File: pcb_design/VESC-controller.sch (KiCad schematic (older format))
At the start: 33 parts, among them J1 GATE_DRIVER_CONN_U, J2 GATE_DRIVER_CONN_V, J3 GATE_DRIVER_CONN_W, J4 micro USB, J5 ACCEL, J6 REGEN, J7 12V, J8 V_BUS, P1 HALL/Encoder, P101 CANBUS, P2 Resolver, P3 PWR_COMM

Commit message: Completed some part numbers
Signed-off-by: Marcos Chaparro <mchaparro@paltatech.com>
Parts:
- C66, C67, C68: MFR (none) -> Murata Electronics North America; MPN (none) -> GRM21BR71A475KA73K; SPN (none) -> 490-6479-1-ND; SPR (none) -> Digikey
- C69, C70, C71: MFR (none) -> Murata Electronics North America; MPN (none) -> GRM31CR71H475KA12L; SPN (none) -> 490-6521-1-ND; SPR (none) -> Digikey

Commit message: Completed part number, manufacturer, etc fields. Simulated analog conditioning
Signed-off-by: Marcos Chaparro <mchaparro@paltatech.com>
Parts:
- D21, D22: MFR (none) -> Toshiba Semiconductor and Storage; MPN (none) -> TBAT54S,LM; SPN (none) -> TBAT54SLMCT-ND; SPR (none) -> Digikey
- DS1, DS5: MFR (none) -> Lite-On Inc.; MPN (none) -> LTST-C191KRKT; SPN (none) -> 160-1447-1-ND; SPR (none) -> Digikey
- DS2, DS4: MFR (none) -> Lite-On Inc.; MPN (none) -> LTST-C191KGKT; SPN (none) -> 160-1446-1-ND; SPR (none) -> Digikey
- J1, J2, J3: MFR (none) -> Amphenol FCI; MPN (none) -> 67997-216HLF; SPN (none) -> 609-3238-ND; SPR (none) -> Digikey
- J4: MFR (none) -> Amphenol FCI; MPN (none) -> 10118194-0001LF; SPN (none) -> 609-4618-1-ND; SPR (none) -> Digikey
- J5, J6: MFR (none) -> Phoenix Contact; MPN (none) -> 1803439; SPN (none) -> 277-1222-ND; SPR (none) -> Digikey
- J7: MFR (none) -> Phoenix Contact; MPN (none) -> 1803426; SPN (none) -> 277-1221-ND; SPR (none) -> Digikey
- J8: MFR (none) -> Phoenix Contact; MPN (none) -> 1803442; SPN (none) -> 277-1223-ND; SPR (none) -> Digikey
- P1, P2: MFR (none) -> Phoenix Contact; MPN (none) -> 1803468; SPN (none) -> 277-1225-ND; SPR (none) -> Digikey
- P101: MFR (none) -> JST Sales America Inc.; MPN (none) -> B4B-PH-K-S(LF)(SN); SPN (none) -> 455-1706-ND; SPR (none) -> Digikey
- P3: MFR (none) -> Phoenix Contact; MPN (none) -> 1803471; SPN (none) -> 277-1226-ND; SPR (none) -> Digikey
- R103, R104: MFR (none) -> Yageo; MPN (none) -> RC0603FR-0722RL; SPN (none) -> 311-22.0HRCT-ND; SPR (none) -> Digikey
- R11, R134, R135, R38: MFR (none) -> Yageo; MPN (none) -> RC0603FR-07100RL; SPN (none) -> 311-100HRCT-ND; SPR (none) -> Digikey
- R139: MFR (none) -> Yageo; MPN (none) -> RC0603FR-071KL; SPN (none) -> 311-1.00KHRCT-ND; SPR (none) -> Digikey
- R140: MFR (none) -> Yageo; MPN (none) -> RC0603FR-0710KL; SPN (none) -> 311-10.0KHRCT-ND; SPR (none) -> Digikey
- R6: MFR (none) -> Yageo; MPN (none) -> RC0603JR-070RL; SPN (none) -> 311-0.0GRCT-ND; SPR (none) -> Digikey

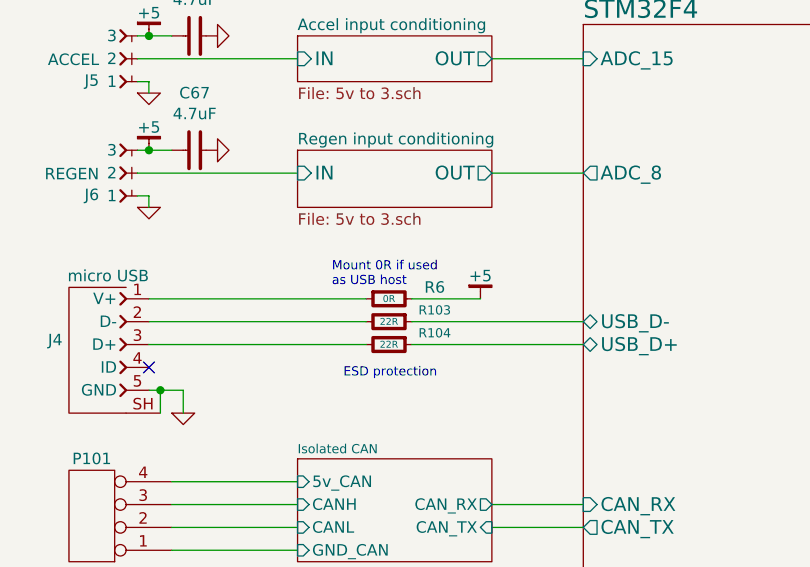
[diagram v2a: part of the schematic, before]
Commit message: Corrected phase current gain. More 3d models
Signed-off-by: Marcos Chaparro <mchaparro@paltatech.com>
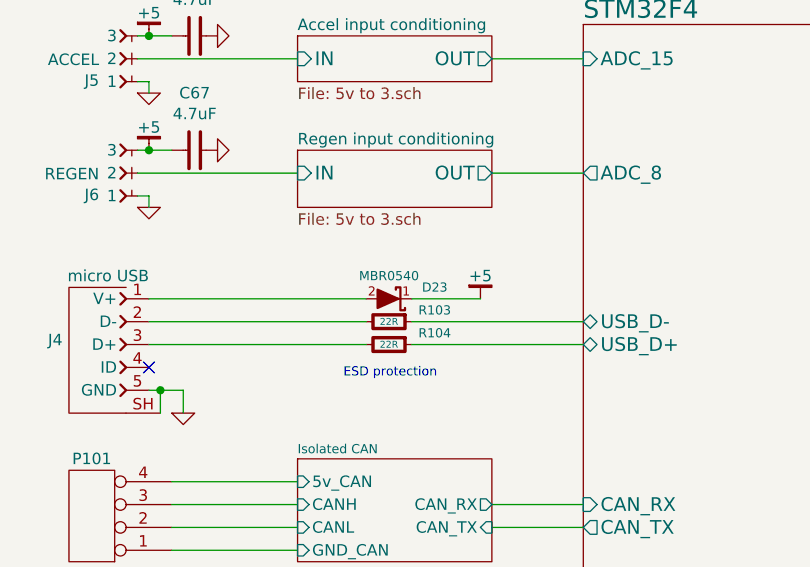
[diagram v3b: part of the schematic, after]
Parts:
- removed R6: 0R, IPC7351-Nominal:RESC1608X50, symbol R-0603
- added D23: MBR0540, smd-semi:SOD-123, symbol MBR0540
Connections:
- net +5: now also D23.1 (K)
- net at J4.1 (V+): now also D23.2 (A)
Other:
- note removed: "Mount 0R if used\nas USB host"

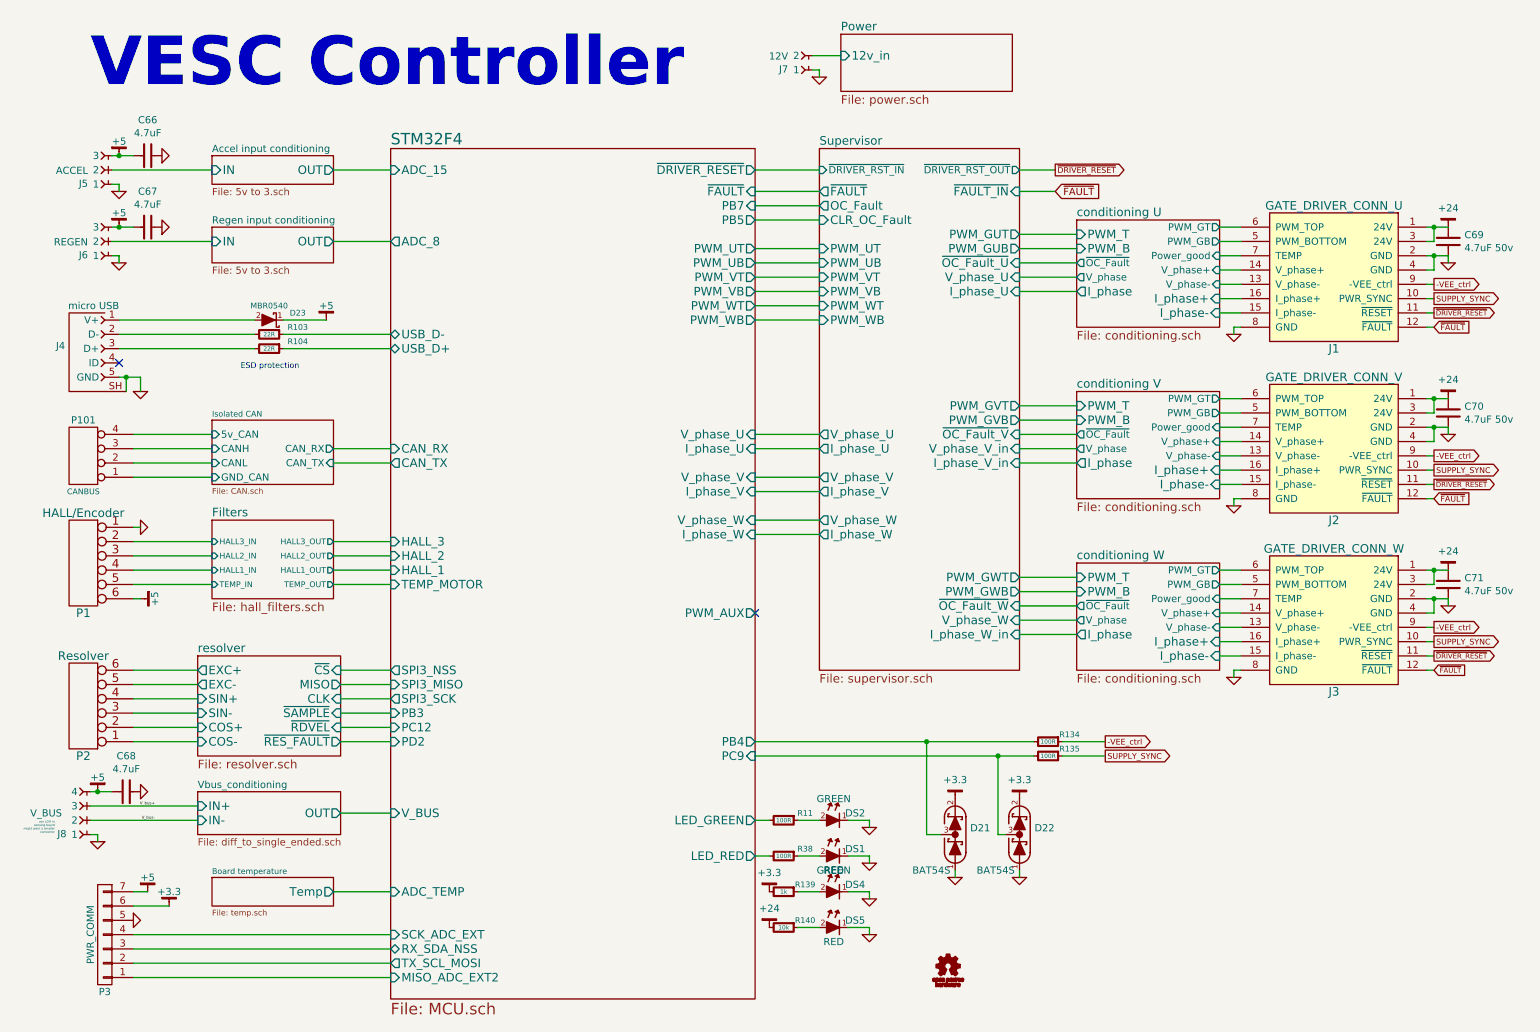
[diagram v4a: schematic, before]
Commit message: Added individual temperature sensing for each half bridge and 2 pwm gpio with low side driver
Signed-off-by: Marcos Chaparro <mchaparro@paltatech.com>
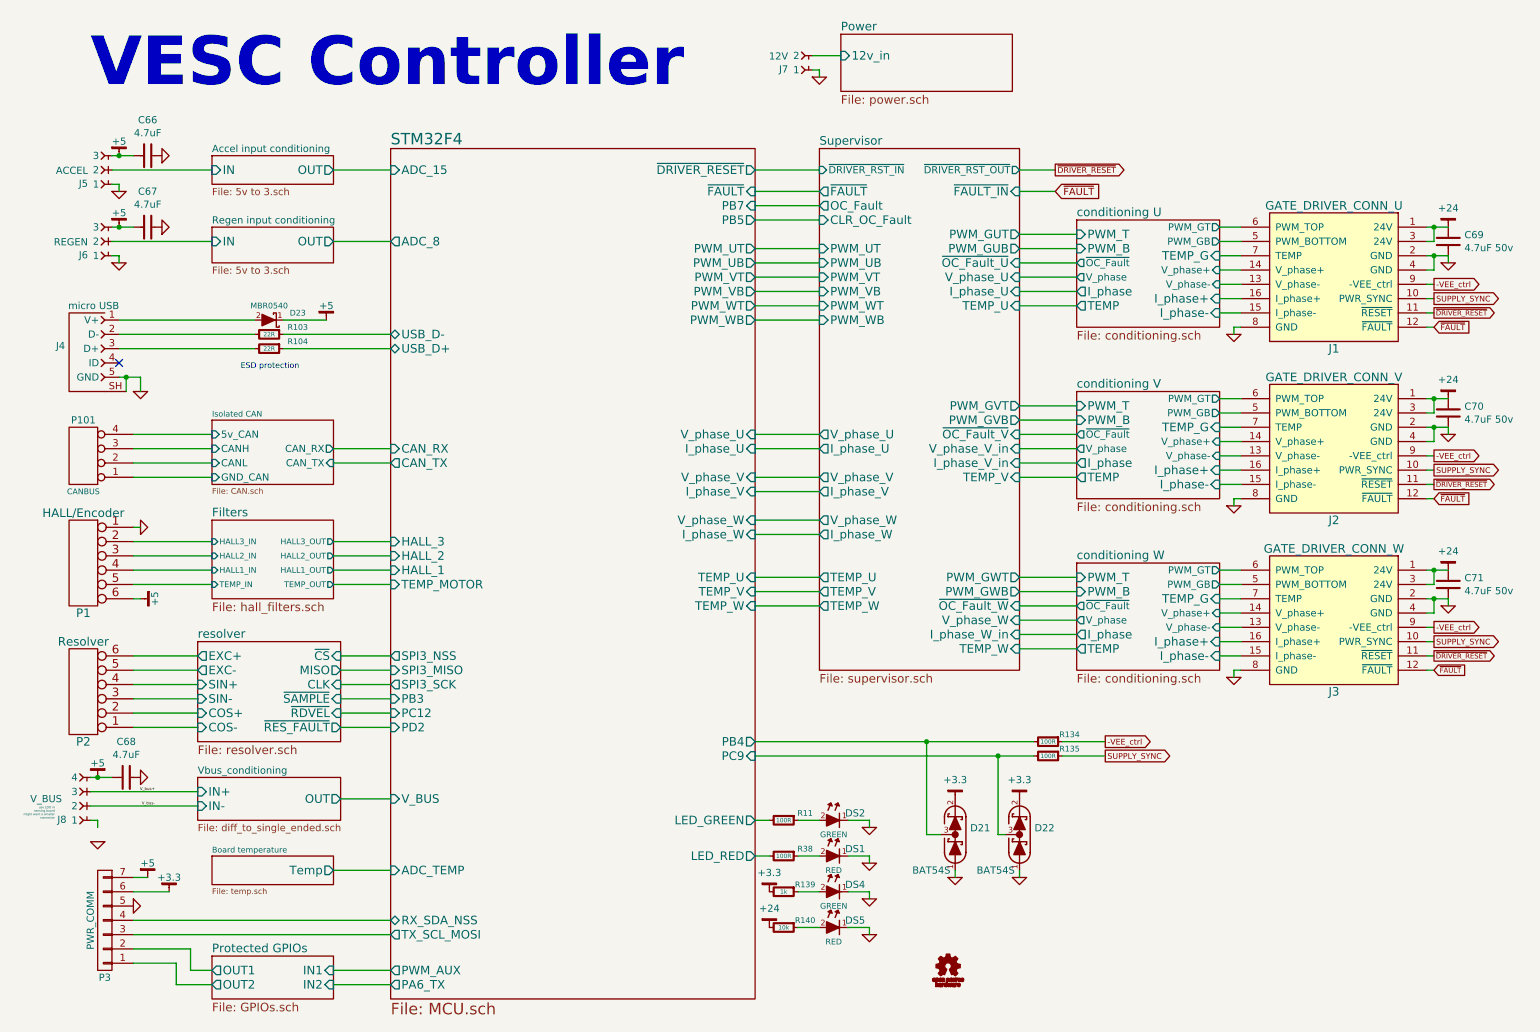
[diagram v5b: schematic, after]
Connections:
- net STM32F4/SCK_ADC_EXT is gone; now on net STM32F4/RX_SDA_NSS: P3.4 (P4)
- net GND: no longer J8.1
- net STM32F4/RX_SDA_NSS: no longer P3.3 (P3)
- net STM32F4/TX_SCL_MOSI: now also P3.3 (P3); no longer P3.2 (P2)
- net STM32F4/MISO_ADC_EXT2 renamed Protected GPIOs/OUT2
- net conditioning U/Power_good renamed conditioning U/TEMP_G
- net conditioning V/Power_good renamed conditioning V/TEMP_G
- net conditioning W/Power_good renamed conditioning W/TEMP_G
- new net Protected GPIOs/OUT1: P3.2 (P2)
- no-connect marks 2 -> 1
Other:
- moved on the sheet: C68, J8, P2, P3

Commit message: Fixed power supply inductor footprints in the layout
Signed-off-by: Marcos Chaparro <mchaparro@paltatech.com>
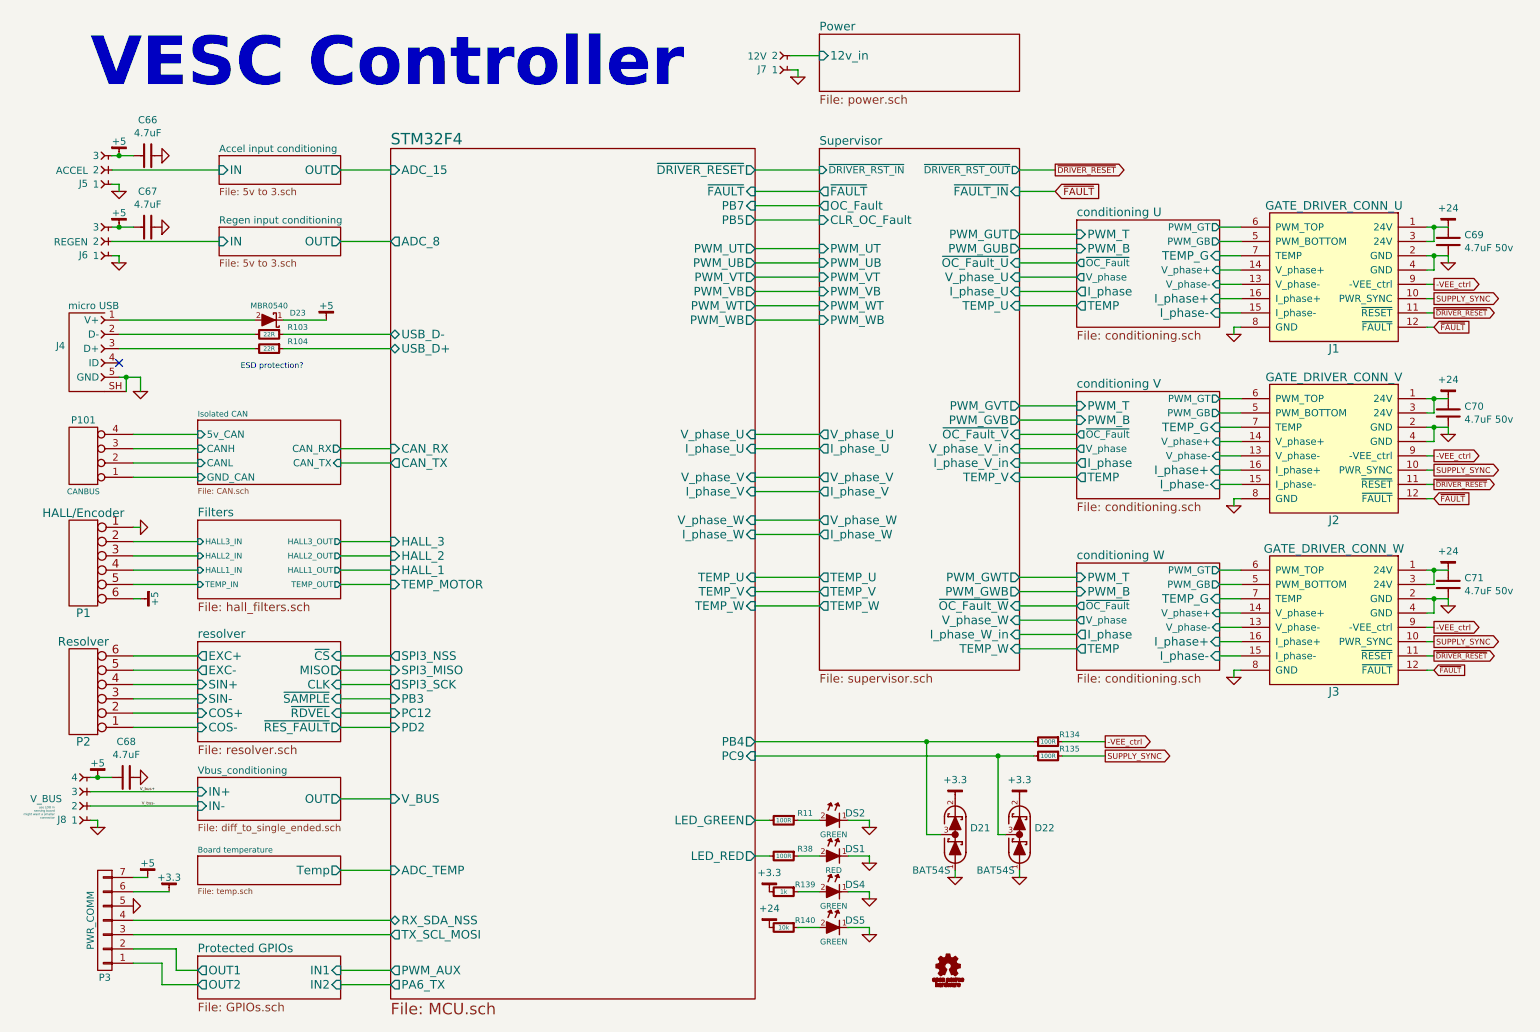
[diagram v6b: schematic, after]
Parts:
- DS5: value RED -> GREEN; MPN LTST-C191KRKT -> LTST-C191KGKT; SPN 160-1447-1-ND -> 160-1446-1-ND
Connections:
- net GND: now also J8.1
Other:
- note added: "ESD protection?"
- note removed: "ESD protection\n"
- moved on the sheet: J7

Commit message: Added RC filter to FAULT line to prevent noise triggering it
Signed-off-by: Marcos Chaparro <mchaparro@paltatech.com>
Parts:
- R103, R104: BOM (none) -> RES SMD 22 1% [0603]; mfg# RC0603FR-0722RL -> (none)
- R11, R134, R135, R38: BOM (none) -> RES SMD 1k 5% [0603]; mfg# RC0603FR-07100RL -> (none)
- R139, R140: BOM (none) -> RES SMD 1k 5% [0603]
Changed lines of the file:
@@
 F 2 "IPC7351-Nominal:RESC1608X50" V 2330 2750 30  0001 C CNN
 F 3 "" H 2400 2750 30  0001 C CNN
-F 4 "RC0603FR-0722RL" H 2400 2750 60  0001 C CNN "mfg#"
+F 4 "" H 2400 2750 60  0001 C CNN "mfg#"
 F 5 "Yageo" H 0   0   50  0001 C CNN "MFR"
 F 6 "RC0603FR-0722RL" H 0   0   50  0001 C CNN "MPN"
@@
 F 8 "311-22.0HRCT-ND" H 0   0   50  0001 C CNN "SPN"
 F 9 "" H 0   0   50  0001 C CNN "SPURL"
+F 10 "RES SMD 22 1% [0603]" H 0   0   60  0001 C CNN "BOM"
 	1    2400 2750
 	0    1    1    0
@@
 F 2 "IPC7351-Nominal:RESC1608X50" V 2330 2850 30  0001 C CNN
 F 3 "" H 2400 2850 30  0001 C CNN
-F 4 "RC0603FR-0722RL" H 2400 2850 60  0001 C CNN "mfg#"
+F 4 "" H 2400 2850 60  0001 C CNN "mfg#"
 F 5 "Yageo" H 0   0   50  0001 C CNN "MFR"
 F 6 "RC0603FR-0722RL" H 0   0   50  0001 C CNN "MPN"
@@
 F 8 "311-22.0HRCT-ND" H 0   0   50  0001 C CNN "SPN"
 F 9 "" H 0   0   50  0001 C CNN "SPURL"
+F 10 "RES SMD 22 1% [0603]" H 0   0   60  0001 C CNN "BOM"
 	1    2400 2850
 	0    1    1    0
@@
 F 2 "IPC7351-Nominal:RESC1608X50" V 5930 6400 30  0001 C CNN
 F 3 "http://www.yageo.com/NewPortal/yageodocoutput?fileName=/pdf/R-Chip/PYu-RC_Group_51_RoHS_L_4.pdf" H 6000 6400 30  0001 C CNN
-F 4 "RC0603FR-07100RL" H 6000 6400 60  0001 C CNN "mfg#"
+F 4 "" H 6000 6400 60  0001 C CNN "mfg#"
 F 5 "Yageo" H 0   0   50  0001 C CNN "MFR"
 F 6 "RC0603FR-07100RL" H 0   0   50  0001 C CNN "MPN"
@@
 F 8 "311-100HRCT-ND" H 0   0   50  0001 C CNN "SPN"
 F 9 "" H 0   0   50  0001 C CNN "SPURL"
+F 10 "RES SMD 1k 5% [0603]" H 0   0   60  0001 C CNN "BOM"
 	1    6000 6400
 	0    1    1    0
@@
 F 2 "IPC7351-Nominal:RESC1608X50" V 5930 6150 30  0001 C CNN
 F 3 "http://www.yageo.com/NewPortal/yageodocoutput?fileName=/pdf/R-Chip/PYu-RC_Group_51_RoHS_L_4.pdf" H 6000 6150 30  0001 C CNN
-F 4 "RC0603FR-07100RL" H 6000 6150 60  0001 C CNN "mfg#"
+F 4 "" H 6000 6150 60  0001 C CNN "mfg#"
 F 5 "Yageo" H 0   0   50  0001 C CNN "MFR"
 F 6 "RC0603FR-07100RL" H 0   0   50  0001 C CNN "MPN"
@@
 F 8 "311-100HRCT-ND" H 0   0   50  0001 C CNN "SPN"
 F 9 "" H 0   0   50  0001 C CNN "SPURL"
+F 10 "RES SMD 1k 5% [0603]" H 0   0   60  0001 C CNN "BOM"
 	1    6000 6150
 	0    1    1    0
@@
 F 2 "IPC7351-Nominal:RESC1608X50" V 7780 5700 30  0001 C CNN
 F 3 "http://www.yageo.com/NewPortal/yageodocoutput?fileName=/pdf/R-Chip/PYu-RC_Group_51_RoHS_L_4.pdf" H 7850 5700 30  0001 C CNN
-F 4 "RC0603FR-07100RL" H 7850 5700 60  0001 C CNN "mfg#"
+F 4 "" H 7850 5700 60  0001 C CNN "mfg#"
 F 5 "Yageo" H 0   0   50  0001 C CNN "MFR"
 F 6 "RC0603FR-07100RL" H 0   0   50  0001 C CNN "MPN"
@@
 F 8 "311-100HRCT-ND" H 0   0   50  0001 C CNN "SPN"
 F 9 "" H 0   0   50  0001 C CNN "SPURL"
+F 10 "RES SMD 1k 5% [0603]" H 0   0   60  0001 C CNN "BOM"
 	1    7850 5700
 	0    1    1    0
@@
 F 2 "IPC7351-Nominal:RESC1608X50" V 7780 5600 30  0001 C CNN
 F 3 "http://www.yageo.com/NewPortal/yageodocoutput?fileName=/pdf/R-Chip/PYu-RC_Group_51_RoHS_L_4.pdf" H 7850 5600 30  0001 C CNN
-F 4 "RC0603FR-07100RL" H 7850 5600 60  0001 C CNN "mfg#"
+F 4 "" H 7850 5600 60  0001 C CNN "mfg#"
 F 5 "Yageo" H 0   0   50  0001 C CNN "MFR"
 F 6 "RC0603FR-07100RL" H 0   0   50  0001 C CNN "MPN"
@@
 F 8 "311-100HRCT-ND" H 0   0   50  0001 C CNN "SPN"
 F 9 "" H 0   0   50  0001 C CNN "SPURL"
+F 10 "RES SMD 1k 5% [0603]" H 0   0   60  0001 C CNN "BOM"
 	1    7850 5600
 	0    1    1    0
@@
 F 7 "311-10.0KHRCT-ND" H 0   0   50  0001 C CNN "SPN"
 F 8 "" H 0   0   50  0001 C CNN "SPURL"
+F 9 "RES SMD 1k 5% [0603]" H 0   0   60  0001 C CNN "BOM"
 	1    6000 6900
 	0    1    1    0
@@
 F 7 "311-1.00KHRCT-ND" H 0   0   50  0001 C CNN "SPN"
 F 8 "" H 0   0   50  0001 C CNN "SPURL"
+F 9 "RES SMD 1k 5% [0603]" H 0   0   60  0001 C CNN "BOM"
 	1    6000 6650
 	0    1    1    0
